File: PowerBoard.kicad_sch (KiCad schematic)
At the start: 102 parts, among them J1 XT90, J10 DEAN_T, J11 DEAN_T, J12 DEAN_T, J13 DEAN_T, J14 DEAN_T, J15 DEAN_T, J16 XT60, J17 XT60, J18 XT60, J19 XT60, J2 DEAN_T, J20 XT60, J21 XT60, J22 XT30, J23 XT30, J24 XT30, J25 XT30, J26 XT30, J27 XT30, J28 XT90, J29 XT30, J3 XT60, J30 XT30, J31 XT30, J32 Conn_01x02, J4 XT30, J5 XT90, J6 XT90, J7 XT90, J8 XT90, J9 XT90, Q1 IRFS7437TRLPBF, Q2 IRFS7437TRLPBF, Q3 IRFS7437TRLPBF, Q6 BC817, Q8 BC817, U1 Pico, U2 LM317_TO-220

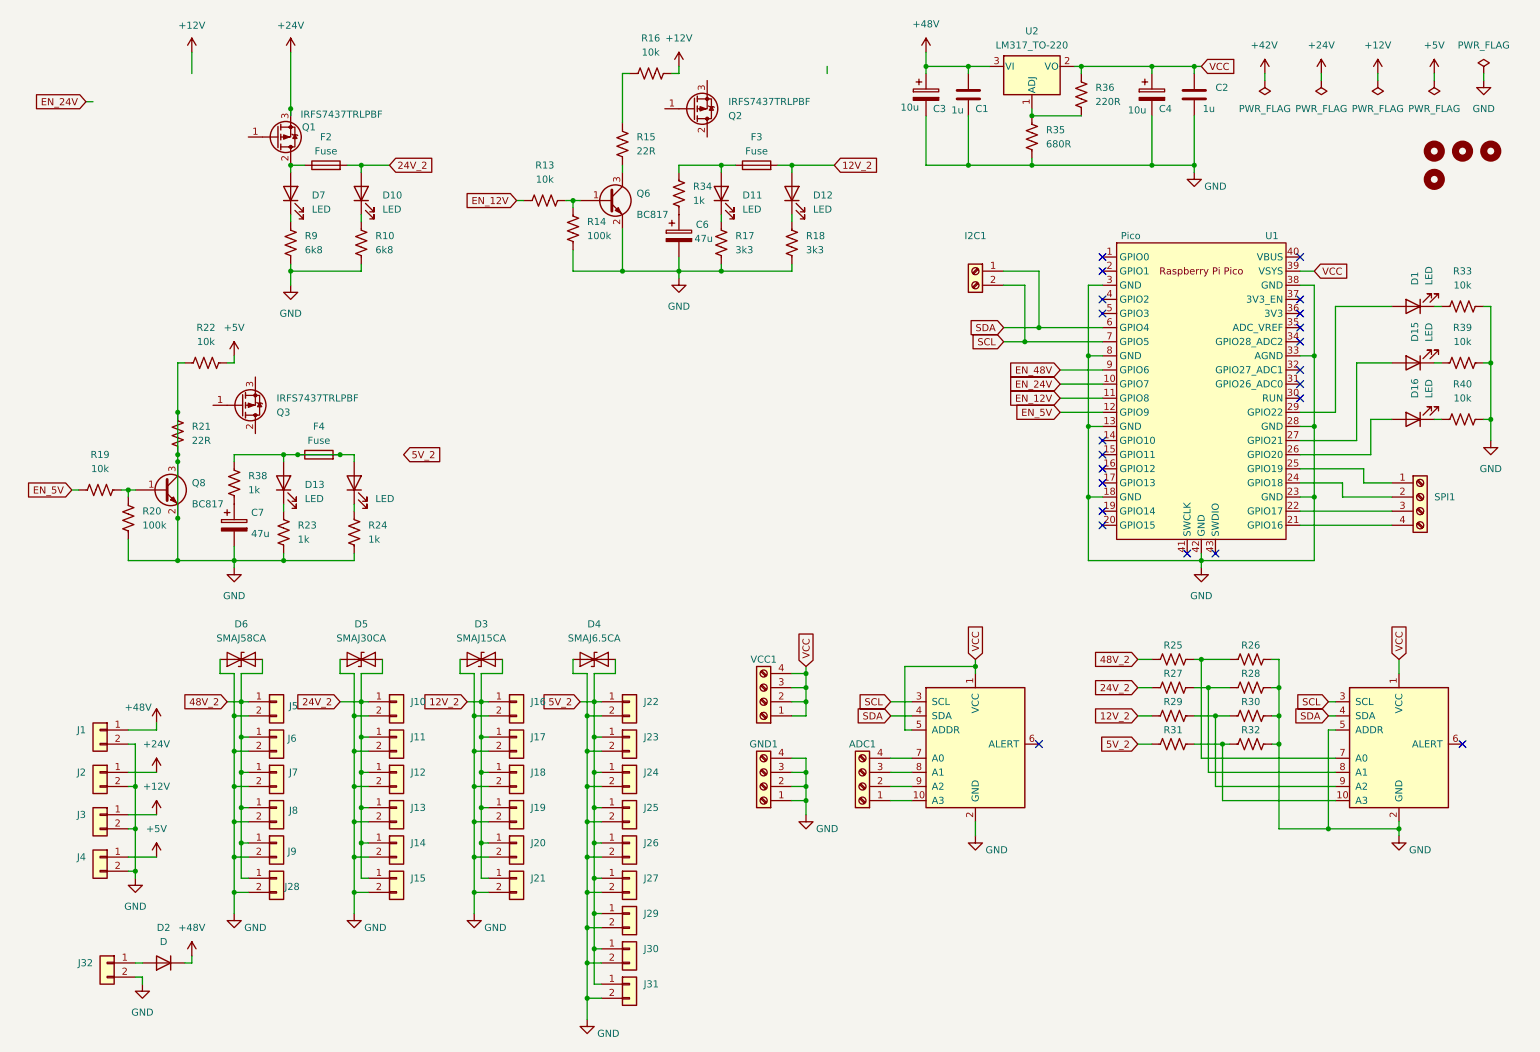
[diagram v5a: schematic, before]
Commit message: Add LTC7004 driver
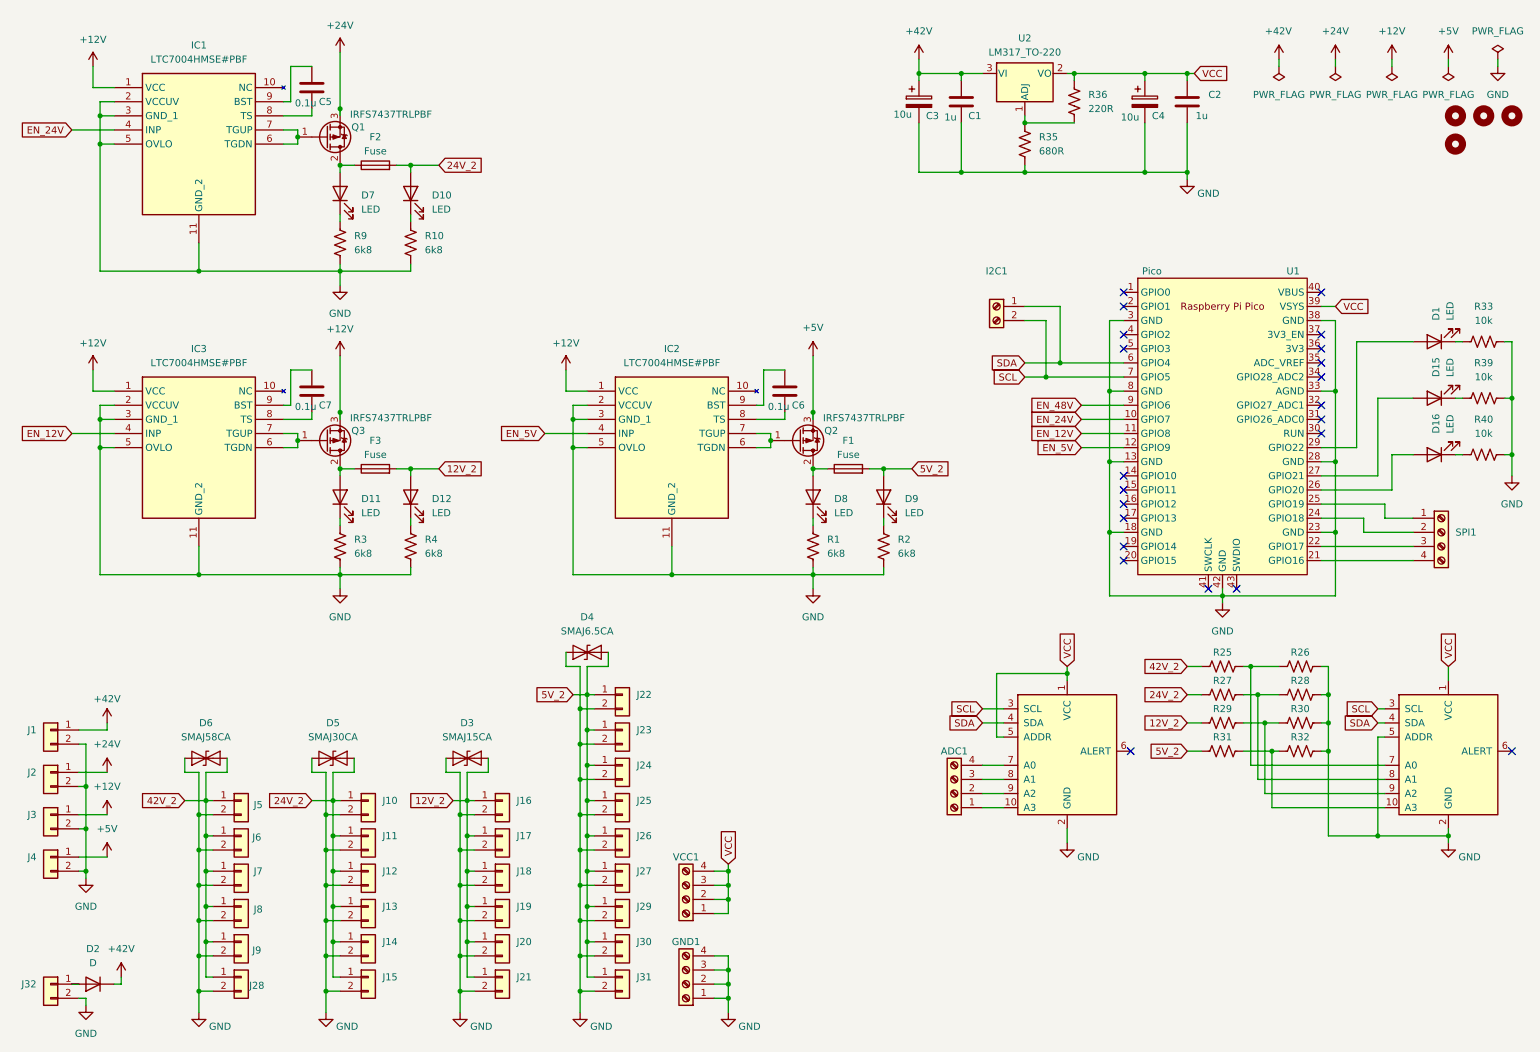
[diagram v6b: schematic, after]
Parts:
- removed C6, C7: 47u, Capacitor_THT:CP_Radial_D6.3mm_P2.50mm, symbol Device:C_Polarized
- removed D13, D14: LED, Diode_SMD:D_1206_3216Metric, symbol Device:LED
- removed F4: Fuse, Fuse:Fuse_Blade_ATO_directSolder, symbol Device:Fuse
- removed Q6, Q8: BC817, Package_TO_SOT_SMD:SOT-23, symbol Transistor_BJT:BC817
- removed R13, R16, R19, R22: 10k, Resistor_SMD:R_1206_3216Metric, symbol Device:R_US
- removed R14, R20: 100k, Resistor_SMD:R_1206_3216Metric, symbol Device:R_US
- removed R15, R21: 22R, Resistor_SMD:R_1206_3216Metric, symbol Device:R_US
- removed R17, R18: 3k3, Resistor_SMD:R_1206_3216Metric, symbol Device:R_US
- removed R23, R24, R34, R38: 1k, Resistor_SMD:R_1206_3216Metric, symbol Device:R_US
- added C5, C6, C7: 0.1u, Capacitor_SMD:C_1206_3216Metric, symbol Device:C
- added D8, D9: LED, Diode_SMD:D_1206_3216Metric, symbol Device:LED
- added F1: Fuse, Fuse:Fuse_Blade_ATO_directSolder, symbol Device:Fuse
- added IC1, IC2, IC3: LTC7004HMSE#PBF, SOP50P490X110-11N, symbol SamacSys_Parts:LTC7004HMSE#PBF
- added R1, R2, R3, R4: 6k8, Resistor_SMD:R_1206_3216Metric, symbol Device:R_US
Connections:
- net +48V is gone; now on net +42V: C1.1, C3.1, D2.1 (K), J1.1 (Pin_1), U2.3 (VI)
- net +12V: now also Q3.3 (S), IC1.1 (VCC), IC2.1 (VCC), IC3.1 (VCC)
- net +5V: now also Q2.3 (S)
- net 5V_2: now also D9.2 (A), F1.2
- net EN_12V: now also IC3.4 (INP)
- net EN_24V: now also IC1.4 (INP)
- net EN_5V: now also IC2.4 (INP)
- net GND: now also IC1.11 (GND_2), IC1.2 (VCCUV), IC1.3 (GND_1), IC1.5 (OVLO), IC2.11 (GND_2), IC2.2 (VCCUV), IC2.3 (GND_1), IC2.5 (OVLO), IC3.11 (GND_2), IC3.2 (VCCUV), IC3.3 (GND_1), IC3.5 (OVLO), R1.2, R2.2, R3.2, R4.2
- net at Q3.1 (G): now also IC3.6 (TGDN), IC3.7 (TGUP)
- net at Q3.2 (D): now also D11.2 (A), F3.1
- net at Q2.1 (G): now also IC2.6 (TGDN), IC2.7 (TGUP)
- net at Q2.2 (D): now also D8.2 (A), F1.1
- net at D11.1 (K): now also R3.1
- net at D12.1 (K): now also R4.1
- net at Q1.1 (G): now also IC1.6 (TGDN), IC1.7 (TGUP)
- net 48V_2 renamed 42V_2
- new net: D9.1 (K), R2.1
- new net: C5.2, IC1.8 (TS)
- new net: C5.1, IC1.9 (BST)
- new net: D8.1 (K), R1.1
- new net: C7.1, IC3.9 (BST)
- new net: C7.2, IC3.8 (TS)
- new net: C6.2, IC2.8 (TS)
- new net: C6.1, IC2.9 (BST)
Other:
- moved on the sheet: ADC1, C1, C2, C3, C4, D1, D10, D15, D16, D2, D3, D4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

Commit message: iterate the layoutL
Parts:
- removed D6: SMAJ58CA, Diode_SMD:D_SMA, symbol Diode:SMAJ58CA
- removed D7: LED, Diode_SMD:D_1206_3216Metric, symbol Device:LED
- removed IC1: LTC7004HMSE#PBF, SOP50P490X110-11N, symbol SamacSys_Parts:LTC7004HMSE#PBF
- added C8: 1u, Capacitor_SMD:C_1206_3216Metric, symbol Device:C
- added D13, D14, D17: LED, Diode_SMD:D_1206_3216Metric, symbol Device:LED
- added D6, D7: SMAJ48A, Diode_SMD:D_SMA, symbol Diode:SMAJ48A
- added F4: Fuse, Fuse:Fuse_Blade_ATO_directSolder, symbol Device:Fuse
- added IC1, IC4: LT1910ES8#PBF, SOIC127P599X175-8N, symbol SamacSys_Parts:LT1910ES8#PBF
- added Q4: IRFS7437TRLPBF, Package_TO_SOT_SMD:TO-263-2, symbol Transistor_FET:IRF9540N
- added R5, R6: 6k8, Resistor_SMD:R_1206_3216Metric, symbol Device:R_US
- added R7, R8: 3m, Resistor_SMD:R_Shunt_Isabellenhuette_BVR4026, symbol Device:R_Shunt
- C5: value 0.1u -> 1u
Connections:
- net +24V: now also R8.4; no longer Q1.3 (S)
- net +42V: now also R7.4
- net 24V_2: now also D17.2 (A); no longer D10.2 (A)
- net 42V_2: now also D14.2 (A), F4.2
- net EN_24V: now also IC1.4 (IN)
- net GND: now also C5.2, C8.2, D6.2 (A2), D7.2 (A2), R5.2, R6.2
- net at Q1.1 (G): now also D7.1 (A1), IC1.5 (GATE), IC1.8 (V+), R8.3
- net at C5.1: now also IC1.1 (GND), IC1.2 (TIMER)
- net at F2.1, Q1.2 (D): now also D10.2 (A)
- net at R9.1: now also D10.1 (K)
- net at R10.1: now also D17.1 (K); no longer D10.1 (K)
- net EN_48V renamed EN_42V
- net EN_42V: now also IC4.4 (IN)
- new net: Q4.3 (S), R7.1
- new net: IC4.6 (SENSE), R7.2
- new net: D6.1 (A1), IC4.5 (GATE), IC4.8 (V+), Q4.1 (G), R7.3
- new net: D14.1 (K), R6.1
- new net: D13.2 (A), F4.1, Q4.2 (D)
- new net: IC1.6 (SENSE), R8.2
- new net: C8.1, IC4.1 (GND), IC4.2 (TIMER)
- new net: Q1.3 (S), R8.1
- new net: D13.1 (K), R5.1
- no-connect marks 22 -> 24
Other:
- moved on the sheet: C1, C2, C3, C4, R35, R36, U2

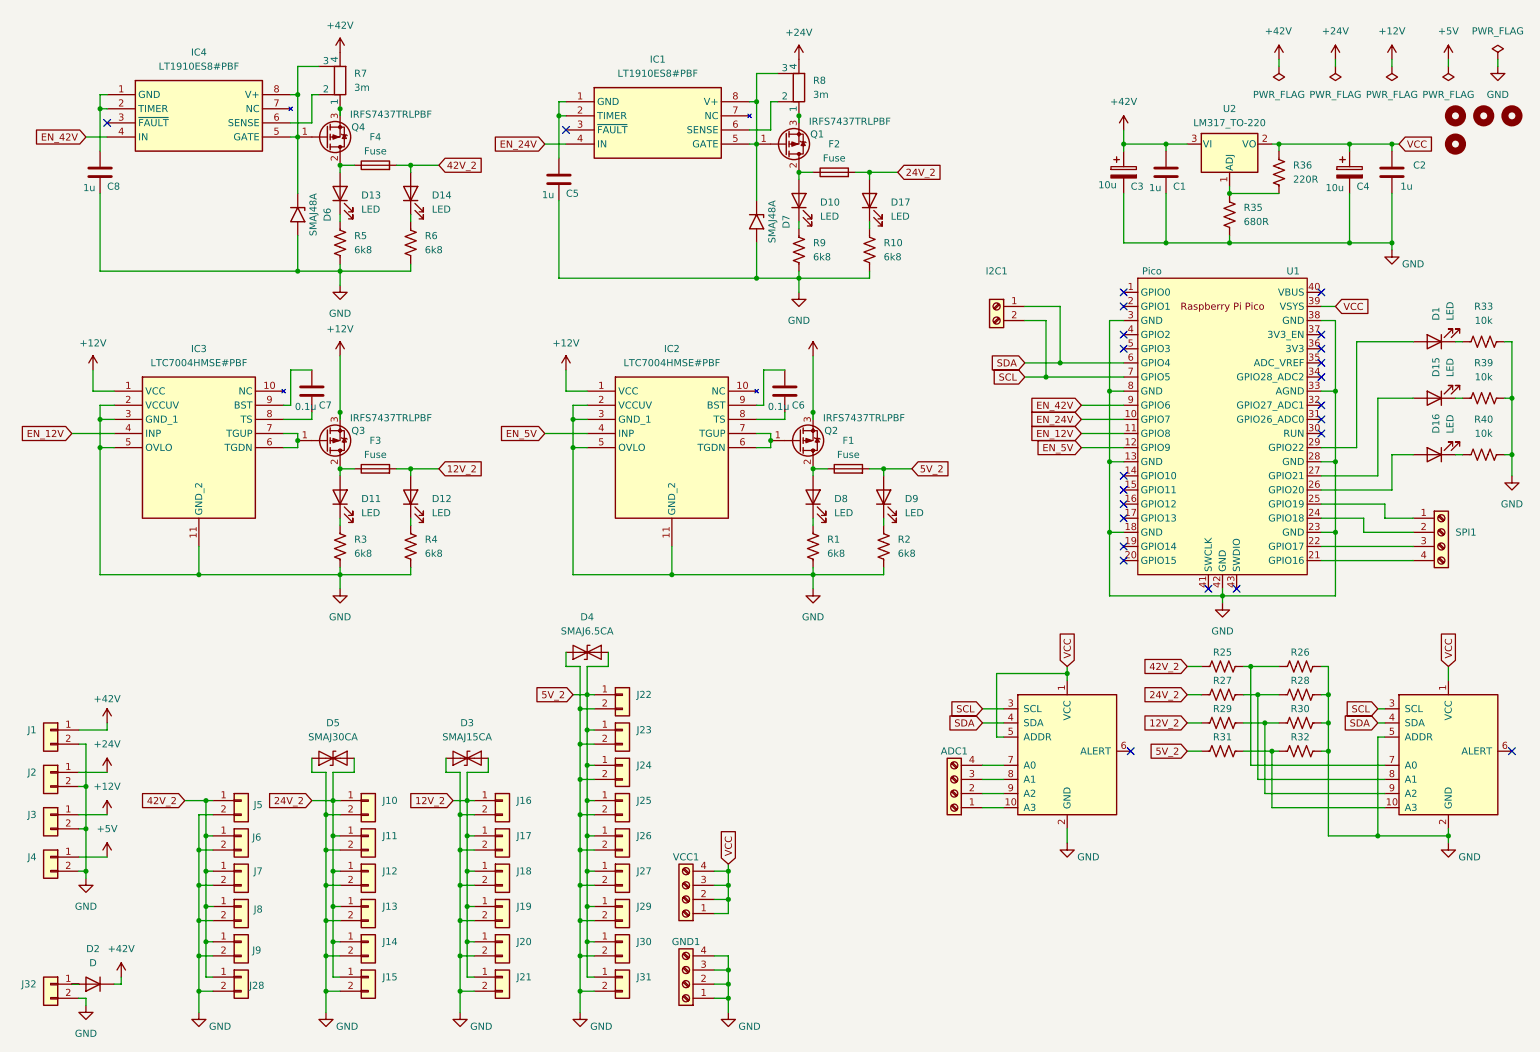
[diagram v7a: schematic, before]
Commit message: fix the layout
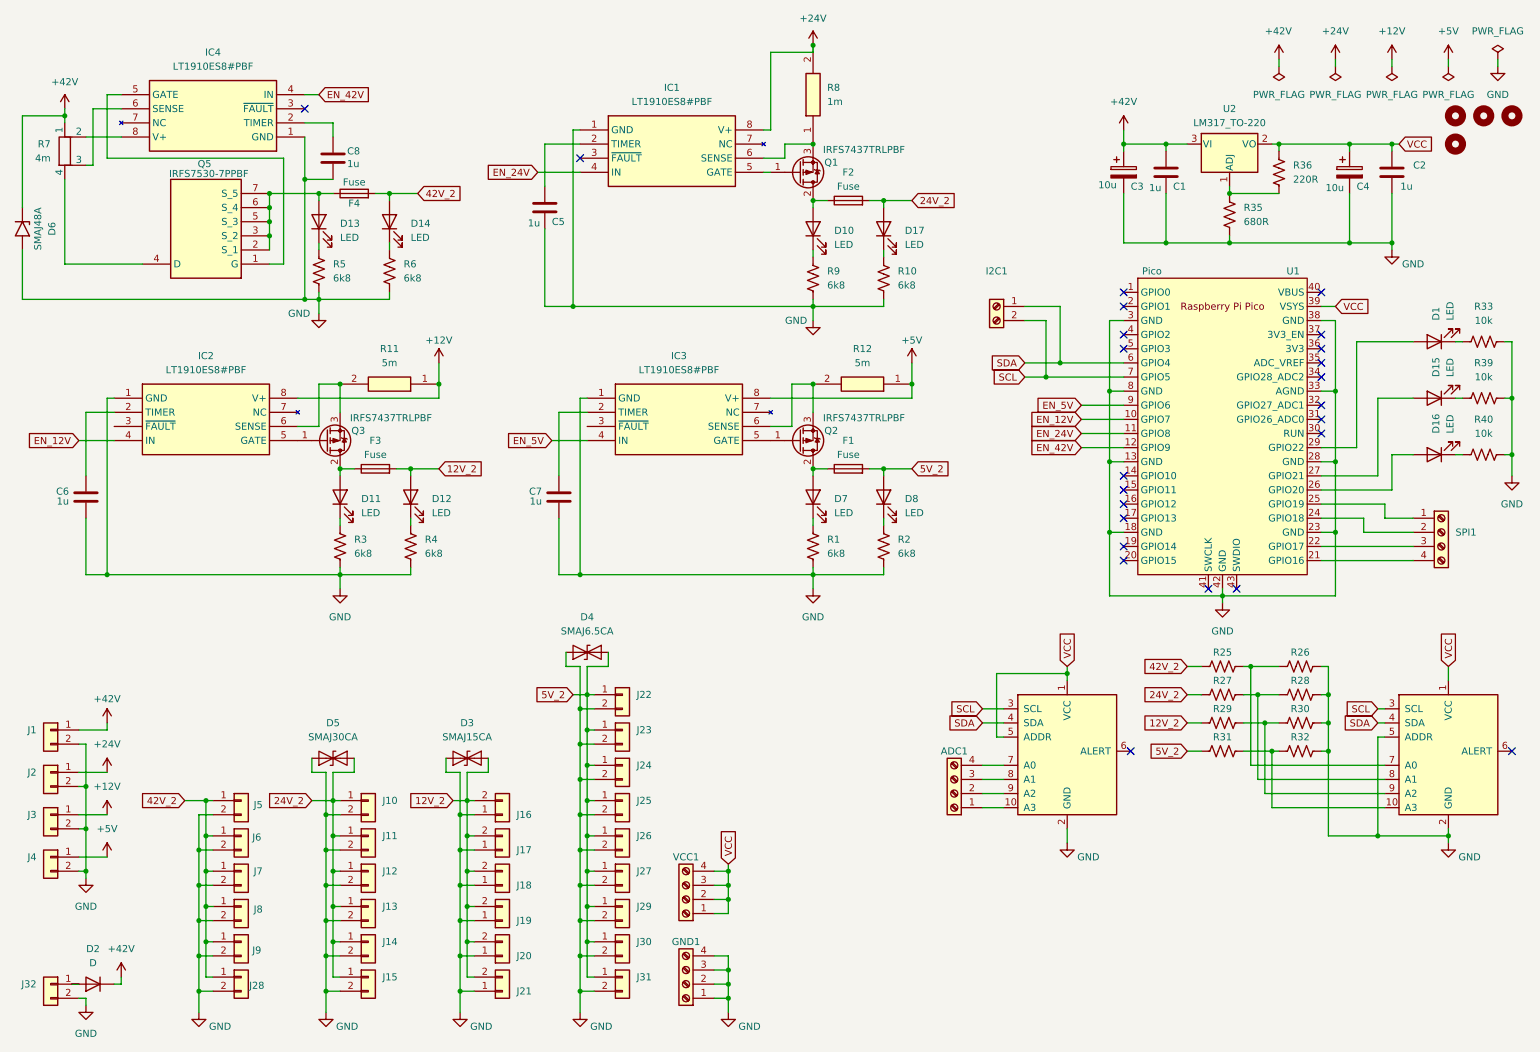
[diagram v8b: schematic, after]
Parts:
- removed D7: SMAJ48A, Diode_SMD:D_SMA, symbol Diode:SMAJ48A
- removed D9: LED, Diode_SMD:D_1206_3216Metric, symbol Device:LED
- removed IC2, IC3: LTC7004HMSE#PBF, SOP50P490X110-11N, symbol SamacSys_Parts:LTC7004HMSE#PBF
- removed Q4: IRFS7437TRLPBF, Package_TO_SOT_SMD:TO-263-2, symbol Transistor_FET:IRF9540N
- removed R8: 3m, Resistor_SMD:R_Shunt_Isabellenhuette_BVR4026, symbol Device:R_Shunt
- added D7: LED, Diode_SMD:D_1206_3216Metric, symbol Device:LED
- added IC2, IC3: LT1910ES8#PBF, SOIC127P599X175-8N, symbol SamacSys_Parts:LT1910ES8#PBF
- added Q5: IRFS7530-7PPBF, IRFS41157PPBF, symbol SamacSys_Parts:IRFS7530-7PPBF
- added R11, R12: 5m, RESC3216X89N, symbol SamacSys_Parts:WSL12061L000FEA
- added R8: 1m, RESC3216X89N, symbol SamacSys_Parts:WSL12061L000FEA
- C6, C7: value 0.1u -> 1u
- J16, J17, J18, J19, J20, J21: footprint my_footprint_lib:XT60 -> Connector_AMASS:AMASS_XT60-F_1x02_P7.20mm_Vertical
- R7: value 3m -> 4m
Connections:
- net +12V: now also IC2.8 (V+), R11.1; no longer Q3.3 (S)
- net +24V: now also IC1.8 (V+), R8.2
- net +42V: now also D6.1 (A1), R7.1; no longer R7.4
- net +5V: now also IC3.8 (V+), R12.1; no longer Q2.3 (S)
- net 12V_2: now also J16.2 (Pin_2), J17.2 (Pin_2), J18.2 (Pin_2), J19.2 (Pin_2), J20.2 (Pin_2), J21.2 (Pin_2); no longer J16.1 (Pin_1), J17.1 (Pin_1), J18.1 (Pin_1), J19.1 (Pin_1), J20.1 (Pin_1), J21.1 (Pin_1)
- net 5V_2: now also D8.2 (A)
- net EN_12V: now also U1.10 (GPIO7), IC2.4 (IN); no longer U1.11 (GPIO8)
- net EN_24V: now also U1.11 (GPIO8); no longer U1.10 (GPIO7)
- net EN_42V: now also U1.12 (GPIO9); no longer U1.9 (GPIO6)
- net EN_5V: now also U1.9 (GPIO6), IC3.4 (IN); no longer U1.12 (GPIO9)
- net GND: now also C6.2, C7.2, IC1.1 (GND), IC4.1 (GND), J16.1 (Pin_1), J17.1 (Pin_1), J18.1 (Pin_1), J19.1 (Pin_1), J20.1 (Pin_1), J21.1 (Pin_1), IC2.1 (GND), IC3.1 (GND); no longer J16.2 (Pin_2), J17.2 (Pin_2), J18.2 (Pin_2), J19.2 (Pin_2), J20.2 (Pin_2), J21.2 (Pin_2)
- net at R7.2: now also IC4.8 (V+); no longer IC4.6 (SENSE)
- net at R2.1: now also D8.1 (K)
- net at R1.1: now also D7.1 (K); no longer D8.1 (K)
- net at F1.1, Q2.2 (D): now also D7.2 (A); no longer D8.2 (A)
- net at D13.2 (A), F4.1: now also Q5.2 (S_1), Q5.3 (S_2), Q5.5 (S_3), Q5.6 (S_4), Q5.7 (S_5)
- net at C5.1, IC1.2 (TIMER): no longer IC1.1 (GND)
- net at IC1.5 (GATE), Q1.1 (G): no longer IC1.8 (V+)
- net at IC1.6 (SENSE): now also Q1.3 (S), R8.1
- net at C8.1, IC4.2 (TIMER): no longer IC4.1 (GND)
- net at C7.1: now also IC3.2 (TIMER)
- net at Q2.1 (G): now also IC3.5 (GATE)
- net at C6.1: now also IC2.2 (TIMER)
- net at Q3.1 (G): now also IC2.5 (GATE)
- new net: IC4.6 (SENSE), R7.3
- new net: Q5.4 (D), R7.4
- new net: IC2.6 (SENSE), Q3.3 (S), R11.2
- new net: IC4.5 (GATE), Q5.1 (G)
- new net: IC3.6 (SENSE), Q2.3 (S), R12.2
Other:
- moved on the sheet: C5, C8, D10, D13, D14, D17, D6, F2, F4, IC1, IC4, Q1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
